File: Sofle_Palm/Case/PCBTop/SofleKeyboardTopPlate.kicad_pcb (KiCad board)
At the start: 2 copper layers, 143.4 x 111.8 mm, 9 parts

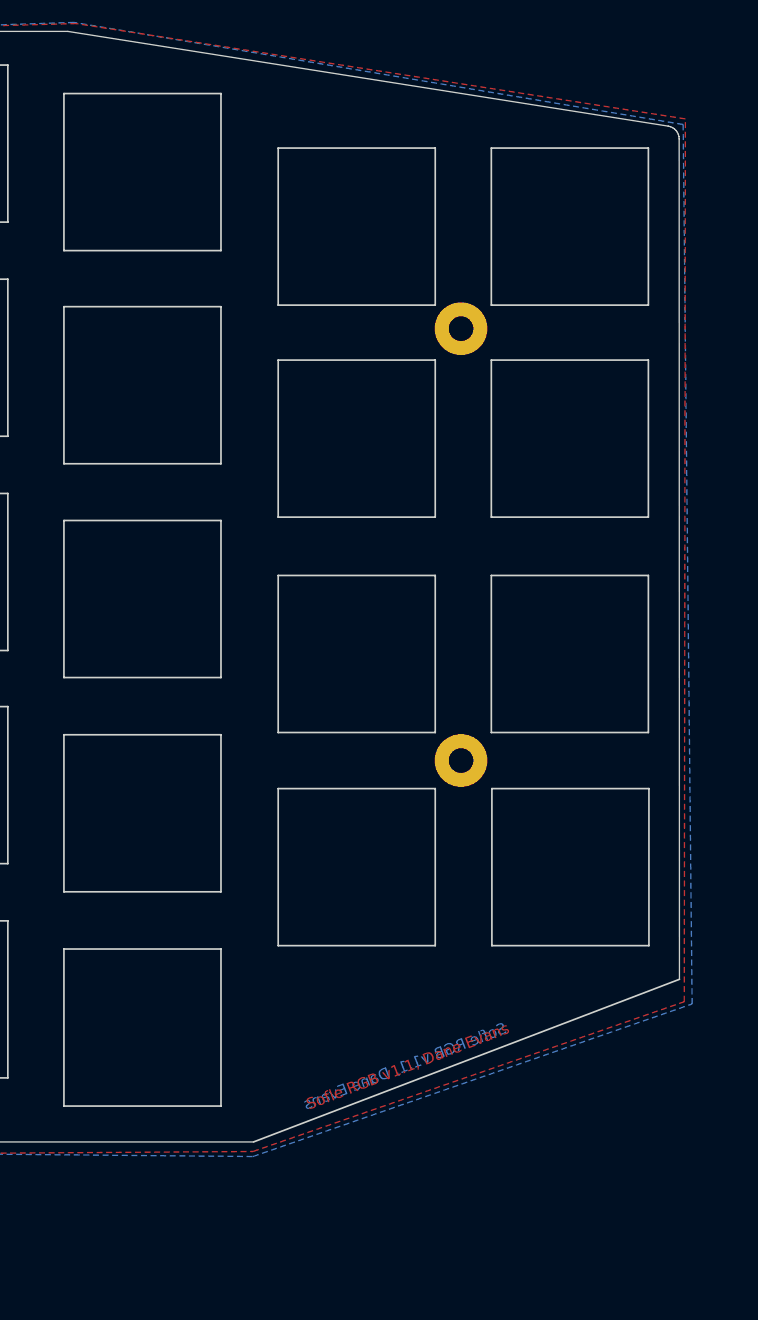
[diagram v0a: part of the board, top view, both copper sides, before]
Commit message: Added new key for Case TOP.
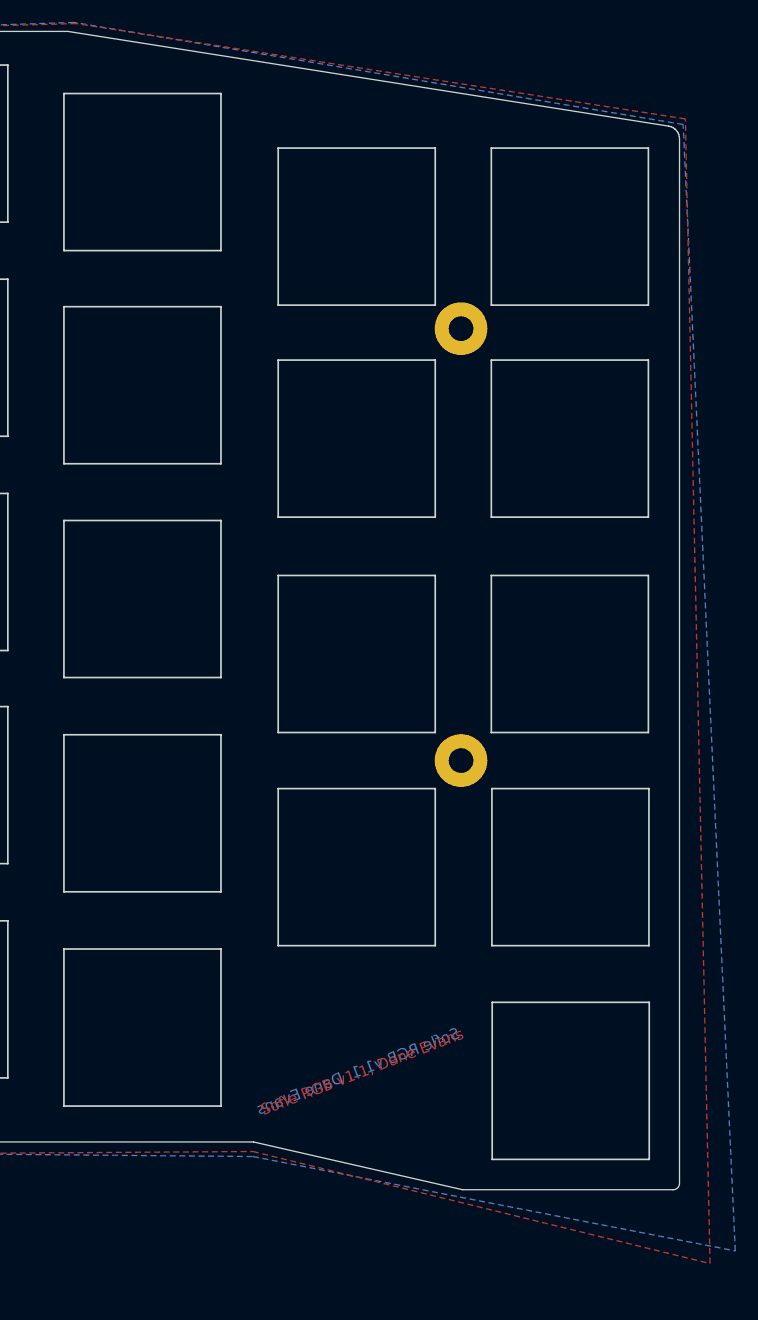
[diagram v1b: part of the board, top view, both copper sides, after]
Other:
- outline, holes or cut-outs redrawn
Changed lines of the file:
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@@
-(kicad_pcb (version 20171130) (host pcbnew "(5.1.6)-1")
+(kicad_pcb (version 20171130) (host pcbnew "(5.1.12-1-10_14)")
   (general
     (thickness 1.6)
-    (drawings 166)
+    (drawings 172)
     (tracks 0)
     (zones 0)
@@
     (0 F.Cu signal)
     (31 B.Cu signal)
-    (32 B.Adhes user hide)
-    (33 F.Adhes user hide)
-    (34 B.Paste user hide)
-    (35 F.Paste user hide)
+    (32 B.Adhes user)
+    (33 F.Adhes user)
+    (34 B.Paste user)
+    (35 F.Paste user)
     (36 B.SilkS user)
     (37 F.SilkS user)
@@
     (uvia_dia 0.3)
     (uvia_drill 0.1)
+  )
+  (module SofleKeyboard-footprint:HOLE_M2_TH (layer F.Cu)
+    (at 207.22 63.22)
+    (fp_text reference TH4 (at 0 -2.54) (layer F.SilkS) hide
+      (effects (font (size 0.29972 0.29972) (thickness 0.0762)))
+    )
+    (fp_text value HOLE (at 0 2.54) (layer F.SilkS) hide
+      (effects (font (size 0.29972 0.29972) (thickness 0.0762)))
+    )
+    (pad "" thru_hole circle (at -0.225 -0.275 90) (size 4.7 4.7) (drill 2.2) (layers *.Cu *.Mask Dwgs.User)
+      (clearance 0.3))
+  )
+  (module SofleKeyboard-footprint:HOLE_M2_TH (layer F.Cu)
+    (at 207.17 101.47)
+    (fp_text reference TH6 (at 0 -2.54) (layer F.SilkS) hide
+      (effects (font (size 0.29972 0.29972) (thickness 0.0762)))
+    )
+    (fp_text value HOLE (at 0 2.54) (layer F.SilkS) hide
+      (effects (font (size 0.29972 0.29972) (thickness 0.0762)))
+    )
+    (pad "" thru_hole circle (at -0.175 -0.025 90) (size 4.7 4.7) (drill 2.2) (layers *.Cu *.Mask Dwgs.User)
+      (clearance 0.3))
   )
   (module dane:gecko-logo (layer F.Cu)
@@
   )
   (module SofleKeyboard-footprint:HOLE_M2_TH (layer F.Cu)
-    (at 207.17 101.47)
-    (fp_text reference TH6 (at 0 -2.54) (layer F.SilkS) hide
-      (effects (font (size 0.29972 0.29972) (thickness 0.0762)))
-    )
-    (fp_text value HOLE (at 0 2.54) (layer F.SilkS) hide
-      (effects (font (size 0.29972 0.29972) (thickness 0.0762)))
-    )
-    (pad "" thru_hole circle (at -0.175 -0.025 90) (size 4.7 4.7) (drill 2.2) (layers *.Cu *.Mask Dwgs.User)
-      (clearance 0.3))
-  )
-  (module SofleKeyboard-footprint:HOLE_M2_TH (layer F.Cu)
     (at 130.97 58.52)
     (fp_text reference TH3 (at 0 -2.54) (layer F.SilkS) hide
@@
     )
     (pad "" thru_hole circle (at 0.025 -0.075 90) (size 4.7 4.7) (drill 2.2) (layers *.Cu *.Mask Dwgs.User)
-      (clearance 0.3))
-  )
-  (module SofleKeyboard-footprint:HOLE_M2_TH (layer F.Cu)
-    (at 207.22 63.22)
-    (fp_text reference TH4 (at 0 -2.54) (layer F.SilkS) hide
-      (effects (font (size 0.29972 0.29972) (thickness 0.0762)))
-    )
-    (fp_text value HOLE (at 0 2.54) (layer F.SilkS) hide
-      (effects (font (size 0.29972 0.29972) (thickness 0.0762)))
-    )
-    (pad "" thru_hole circle (at -0.225 -0.275 90) (size 4.7 4.7) (drill 2.2) (layers *.Cu *.Mask Dwgs.User)
       (clearance 0.3))
   )
@@
       (xy 0.54669 -1.86187) (xy 0.574235 -1.866205) (xy 0.601318 -1.845968)) (layer F.Mask) (width 0.01))
   )
+  (gr_line (start 209.77294 136.99754) (end 209.77294 122.99754) (layer Edge.Cuts) (width 0.15))
+  (gr_line (start 223.77294 136.99754) (end 209.77294 136.99754) (layer Edge.Cuts) (width 0.15))
+  (gr_line (start 209.77294 122.99754) (end 223.77294 122.99754) (layer Edge.Cuts) (width 0.15))
+  (gr_line (start 223.77294 122.99754) (end 223.77294 136.99754) (layer Edge.Cuts) (width 0.15))
+  (gr_arc (start 225.9013 139.13342) (end 225.896221 139.702379) (angle -90.49997641) (layer Edge.Cuts) (width 0.1))
+  (gr_line (start 226.311361 45.440367) (end 226.397761 45.621232) (layer Edge.Cuts) (width 0.1))
+  (gr_line (start 171.945 36.445) (end 225.502921 44.887706) (layer Edge.Cuts) (width 0.1))
+  (gr_line (start 226.470661 46.024462) (end 226.470282 139.133534) (layer Edge.Cuts) (width 0.1))
+  (gr_line (start 226.451861 45.817131) (end 226.470661 46.024462) (layer Edge.Cuts) (width 0.1))
+  (gr_line (start 226.397761 45.621232) (end 226.451861 45.817131) (layer Edge.Cuts) (width 0.1))
+  (gr_line (start 225.704591 44.939336) (end 225.889351 45.024026) (layer Edge.Cuts) (width 0.1))
+  (gr_line (start 225.502921 44.887706) (end 225.704591 44.939336) (layer Edge.Cuts) (width 0.1))
+  (gr_line (start 226.195801 45.278142) (end 226.311361 45.440367) (layer Edge.Cuts) (width 0.1))
+  (gr_line (start 207.13578 139.70238) (end 188.495 135.445) (layer Edge.Cuts) (width 0.1))
+  (gr_line (start 225.889351 45.024026) (end 226.054101 45.13816) (layer Edge.Cuts) (width 0.1))
+  (gr_line (start 225.896221 139.702379) (end 207.13578 139.70238) (layer Edge.Cuts) (width 0.1))
+  (gr_line (start 226.054101 45.13816) (end 226.195801 45.278142) (layer Edge.Cuts) (width 0.1))
   (gr_text "Sofle RGB - Dane Evans\n" (at 101.495 114.3) (layer B.SilkS)
     (effects (font (size 1 1) (thickness 0.2)) (justify mirror))
@@
   (gr_line (start 111.995 96.8) (end 111.995 39.045) (layer Edge.Cuts) (width 0.15))
   (gr_line (start 90.3 97.8) (end 110.995 97.8) (layer Edge.Cuts) (width 0.15))
-  (gr_text "Sofle RGB v1.1, Dane Evans" (at 202.245 128.695 21) (layer F.Cu)
+  (gr_text "Sofle RGB v1.1, Dane Evans" (at 198.17212 129.18932 21) (layer F.Cu)
     (effects (font (size 1 1) (thickness 0.2)))
   )
-  (gr_text "Sofle RGB v1.1, Dane Evans" (at 201.995 128.695 21) (layer B.Cu)
+  (gr_text "Sofle RGB v1.1, Dane Evans" (at 197.81398 129.13852 21) (layer B.Cu)
     (effects (font (size 1 1) (thickness 0.2)) (justify mirror))
   )
@@
     (effects (font (size 1 1) (thickness 0.15)) (justify mirror))
   )
-  (gr_line (start 225.856871 45.026466) (end 226.021621 45.1406) (layer Edge.Cuts) (width 0.1))
   (gr_line (start 89.270257 115.845) (end 89.3 98.8) (layer Edge.Cuts) (width 0.1))
-  (gr_line (start 226.163321 45.280582) (end 226.278881 45.442807) (layer Edge.Cuts) (width 0.1))
   (gr_line (start 149.995 36.445) (end 171.945 36.445) (layer Edge.Cuts) (width 0.1))
-  (gr_line (start 226.021621 45.1406) (end 226.163321 45.280582) (layer Edge.Cuts) (width 0.1))
   (gr_line (start 139.149128 135.445) (end 94.895 148.195) (layer Edge.Cuts) (width 0.1))
   (gr_line (start 83.095 128.345) (end 83.195 127.845) (layer Edge.Cuts) (width 0.1))
@@
   (gr_line (start 139.149128 135.445) (end 188.495 135.445) (layer Edge.Cuts) (width 0.1))
   (gr_line (start 149.995 36.445) (end 113.395 37.9) (layer Edge.Cuts) (width 0.1))
-  (gr_line (start 226.365281 45.623672) (end 226.419381 45.819571) (layer Edge.Cuts) (width 0.1))
   (gr_line (start 83.195 127.845) (end 88.995 117.095) (layer Edge.Cuts) (width 0.1))
-  (gr_line (start 226.419381 45.819571) (end 226.438181 46.026902) (layer Edge.Cuts) (width 0.1))
-  (gr_line (start 226.438181 46.026902) (end 226.465181 120.945) (layer Edge.Cuts) (width 0.1))
-  (gr_line (start 225.470441 44.890146) (end 225.672111 44.941776) (layer Edge.Cuts) (width 0.1))
   (gr_line (start 93.545 147.645) (end 93.895 147.945) (layer Edge.Cuts) (width 0.1))
   (gr_line (start 83.095 128.745) (end 83.095 128.345) (layer Edge.Cuts) (width 0.1))
   (gr_line (start 89.195 116.495) (end 88.995 117.095) (layer Edge.Cuts) (width 0.1))
-  (gr_line (start 226.465181 120.945) (end 188.495 135.445) (layer Edge.Cuts) (width 0.15))
-  (gr_line (start 225.672111 44.941776) (end 225.856871 45.026466) (layer Edge.Cuts) (width 0.1))
   (gr_line (start 93.895 147.945) (end 94.345 148.095) (layer Edge.Cuts) (width 0.1))
   (gr_line (start 83.145 129.345) (end 83.095 128.745) (layer Edge.Cuts) (width 0.1))
   (gr_line (start 94.345 148.095) (end 94.895 148.195) (layer Edge.Cuts) (width 0.1))
   (gr_line (start 89.270257 115.845) (end 89.195 116.495) (layer Edge.Cuts) (width 0.1))
-  (gr_line (start 171.945 36.445) (end 225.470441 44.890146) (layer Edge.Cuts) (width 0.1))
   (gr_line (start 93.545 147.645) (end 83.295 129.845) (layer Edge.Cuts) (width 0.1))
-  (gr_line (start 226.278881 45.442807) (end 226.365281 45.623672) (layer Edge.Cuts) (width 0.1))
   (zone (net 0) (net_name "") (layer F.Cu) (hatch edge 0.508)
     (connect_pads (clearance 0.508))
@@
       (pts
         (xy 81.945 128.645) (xy 93.895 149.095) (xy 138.995 136.395) (xy 158.245 136.495) (xy 188.445 136.295)
-        (xy 226.895 122.945) (xy 226.995 44.245) (xy 172.695 35.745) (xy 88.445 38.045) (xy 88.795 116.445)
+        (xy 229.1906 146.28352) (xy 226.995 44.245) (xy 172.695 35.745) (xy 88.445 38.045) (xy 88.795 116.445)
       )
     )
@@
     (polygon
       (pts
-        (xy 81.845 128.695) (xy 93.595 149.295) (xy 139.095 136.295) (xy 188.445 136.745) (xy 227.595 123.145)
+        (xy 81.845 128.695) (xy 93.595 149.295) (xy 139.095 136.295) (xy 188.445 136.745) (xy 231.44104 145.1583)
         (xy 226.795 44.745) (xy 172.495 35.645) (xy 88.595 38.345) (xy 88.945 116.095)
       )
